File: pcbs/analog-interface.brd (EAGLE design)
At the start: 50 x 50 mm, 26 parts, among them U1 ISL3179EIBZ, U2 ATMEGA328P, U3 LM4120

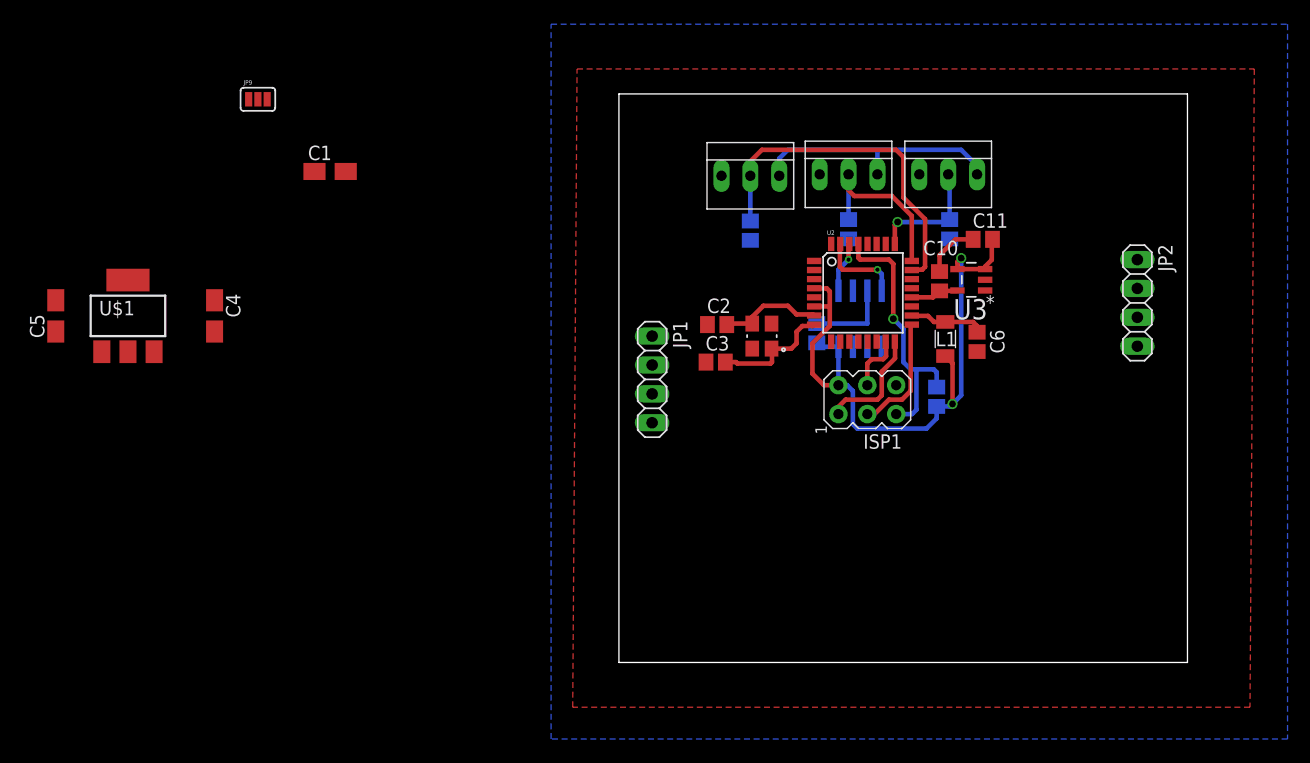
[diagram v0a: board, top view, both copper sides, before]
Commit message: Now uses external ADC and is long and thin.  Possibly too long...
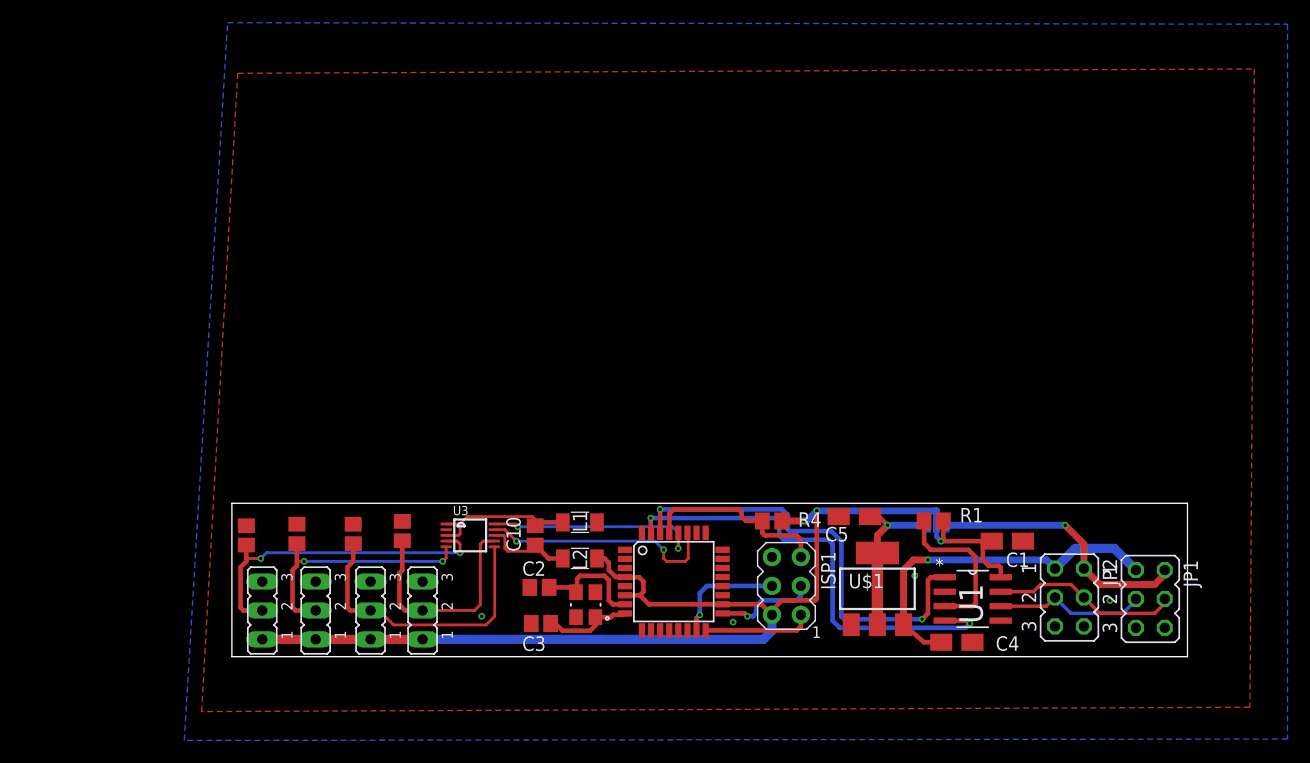
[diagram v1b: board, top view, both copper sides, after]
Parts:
- removed C11: 100nF, resistor:C0805
- added JP6: ADC3, jumper:JP2
- added L2: 10uH, resistor:L3216C
- C10: value 22nF -> 1uF
- C6, C7, C8, C9: value 100uF -> 1uF
- JP1, JP2: device pinhead:1X04 -> jumper:JP3Q
- JP3, JP4, JP5: device farnell-parts:3-MOLEX -> jumper:JP2
- U3: value LM4120 -> (none); device mountainsensing:SOT23-5 -> microbuilder:MSOP10
- moved C5 72.4 mm to (20.7, 12.8), turned to 0 degrees
- moved C4 71.3 mm to (29.7, 1.78), turned to 180 degrees
- moved JP9 70.5 mm to (27.9, 12.1), flipped to the bottom
- moved U$1 70.1 mm to (22.7, 6.48)
- moved C1 67.9 mm to (34.2, 10.7), turned to 180 degrees
- moved JP5 63.7 mm to (-21.8, 4.57), turned to 90 degrees
- moved JP4 60.6 mm to (-26.7, 4.57), turned to 90 degrees
- moved C9 58.9 mm to (-23.4, 11.3), flipped to the top, turned to 270 degrees
- moved JP3 57.5 mm to (-31.4, 4.57), turned to 90 degrees
- moved C8 55.4 mm to (-28.3, 11.3), flipped to the top, turned to 270 degrees
- moved C6 53.2 mm to (-19.1, 11.6), turned to 270 degrees
- moved C7 51.8 mm to (-32.8, 11.2), flipped to the top, turned to 270 degrees
- moved U3 49.5 mm to (-13.1, 11.2), turned to 270 degrees
- moved JP1 47.9 mm to (46.7, 5.59)
- moved C10 42.0 mm to (-7.37, 11.2)
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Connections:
- net 3V3 renamed 5V
- removed net AREF: C10.2, U2.20, U3.5
- removed net VIN: C1.+, C4.+, JP1.1, JP2.1, JP9.1, U$1.3
- new net 12V: C4.+, JP1.1, JP2.1, U$1.3
- new net 5V_IN: JP1.2, JP2.2, JP9.1
- new net ADC3: C6.2, JP6.2, U3.7
- new net SCL: U2.28, U3.10
- new net SDA: U2.27, U3.9
- net 485_N: now also JP1.4, JP2.4; no longer JP1.3, JP2.3
- net 485_P: now also JP1.3, JP2.3; no longer JP1.2, JP2.2
- net ADC0: now also U3.4; no longer U2.23
- net ADC1: now also U3.5; no longer U2.24
- net ADC2: now also U3.6; no longer U2.25
- net GND: now also JP1.5, JP1.6, JP2.5, JP2.6, JP6.3, L1.2; no longer JP1.4, JP2.4, U3.2
- net N$4: now also C10.1, U3.1, U3.3; no longer C6.2, U2.18
- net N$7: now also C10.2, L2.1, U3.8; no longer C10.1, C11.1
- net VCC: now also C1.+, JP6.1, L2.2, U2.18; no longer C11.2, L1.2, U3.3, U3.4
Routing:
- net RX: track 4.51 -> 38.9 mm, vias 1 -> 2
- net TX: track 7.44 -> 40.5 mm, vias 1 -> 2
- net 12V: track 0.00 -> 31.3 mm, vias 0 -> 1
- net VCC: track 81.5 -> 107.6 mm, vias 2 -> 3
- net 5V_IN: track 0.00 -> 23.4 mm, vias 0 -> 1
- net SDA: track 0.00 -> 21.1 mm, vias 0 -> 2
- net ADC3: track 0.00 -> 19.9 mm
- net SCL: track 0.00 -> 19.3 mm, vias 0 -> 2
- net 485_N: track 0.00 -> 16.5 mm
- net ADC2: track 10.7 -> 25.9 mm, vias 1 -> 0
- net 5V: track 0.00 -> 14.5 mm, vias 0 -> 1
- net 485_P: track 0.00 -> 13.4 mm
- net N$4: track 6.67 -> 13.5 mm
- net !RESET: track 23.6 -> 16.9 mm, vias 1 -> 0
- net N$1: track 7.33 -> 13.9 mm
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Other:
- board size 50 x 50 mm -> 84 x 13.5 mm

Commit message: Now has seperate AGND and AVCC 12V available on ADC headers lots of vias A bit shorter
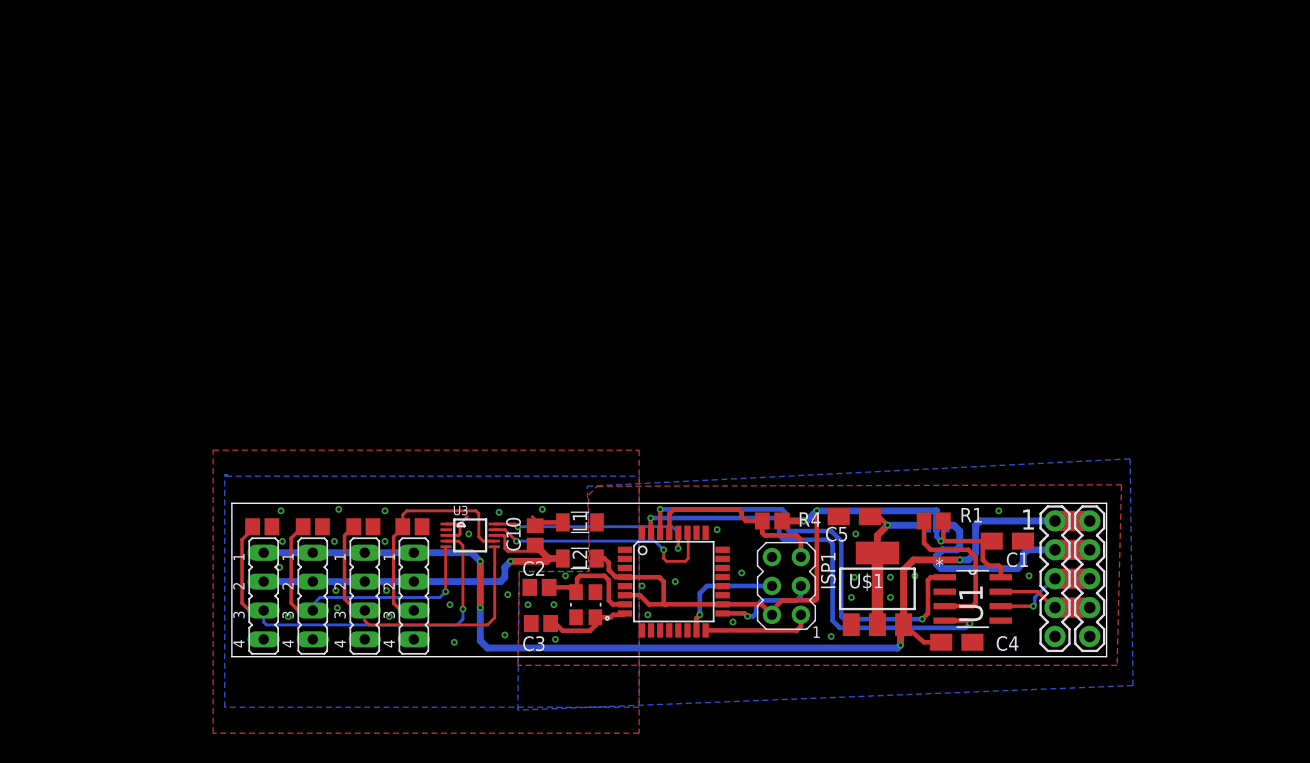
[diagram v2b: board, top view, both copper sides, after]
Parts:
- removed JP1, JP2: (no value), jumper:JP3Q
- added JP7, JP8: (no value), SparkFun-Connectors:1X05
- JP3: value ADC0 -> 0; device jumper:JP2 -> jumper:JP4
- JP4: value ADC1 -> 1; device jumper:JP2 -> jumper:JP4
- JP5: value ADC2 -> 2; device jumper:JP2 -> jumper:JP4
- JP6: value ADC3 -> 3; device jumper:JP2 -> jumper:JP4
- moved C7 1.59 mm to (-31.4, 11.9), turned to 180 degrees
- moved C8 1.53 mm to (-26.9, 11.9), turned to 180 degrees
- moved JP6 1.48 mm to (-18.0, 5.84), turned to 270 degrees
- moved JP5 1.37 mm to (-22.4, 5.84), turned to 270 degrees
- moved JP4 1.30 mm to (-26.9, 5.84), turned to 270 degrees
- moved JP3 1.28 mm to (-31.2, 5.84), turned to 270 degrees
- moved C9 1.09 mm to (-22.5, 11.9), turned to 180 degrees
- moved C6 0.97 mm to (-18.2, 11.9), turned to 180 degrees
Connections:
- removed net 12V: C4.+, JP1.1, JP2.1, U$1.3
- removed net N$4: C10.1, L1.1, U3.1, U3.3
- removed net N$7: C10.2, L2.1, U3.8
- new net 12V_IN: C4.+, JP3.1, JP4.1, JP5.1, JP6.1, JP7.1, JP8.1, U$1.3
- new net AGND: C10.1, C6.1, C7.1, C8.1, C9.1, JP3.4, JP4.4, JP5.4, JP6.4, L1.1, U3.1, U3.3
- new net AVCC: C10.2, JP3.2, JP4.2, JP5.2, JP6.2, L2.1, U3.8
- net 485_N: now also JP7.4, JP8.4; no longer JP1.4, JP2.4
- net 485_P: now also JP7.3, JP8.3; no longer JP1.3, JP2.3
- net 5V_IN: now also JP7.2, JP8.2; no longer JP1.2, JP2.2
- net ADC0: now also JP3.3; no longer JP3.2
- net ADC1: now also JP4.3; no longer JP4.2
- net ADC2: now also JP5.3; no longer JP5.2
- net ADC3: now also JP6.3; no longer JP6.2
- net GND: now also JP7.5, JP8.5; no longer C6.1, C7.1, C8.1, C9.1, JP1.5, JP1.6, JP2.5, JP2.6, JP3.3, JP4.3, JP5.3, JP6.3
- net VCC: no longer JP3.1, JP4.1, JP5.1, JP6.1
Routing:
- net 12V_IN: track 0.00 -> 93.9 mm, vias 0 -> 4
- net VCC: track 107.6 -> 63.5 mm
- net AVCC: track 0.00 -> 35.4 mm, vias 0 -> 1
- net 12V: track 31.3 -> 0.00 mm, vias 1 -> 0
- net N$4: track 13.5 -> 0.00 mm
- net N$7: track 8.22 -> 0.00 mm
- net 485_N: track 16.5 -> 8.40 mm
- net AGND: track 0.00 -> 7.80 mm, vias 0 -> 19
- net ADC0: track 28.8 -> 36.3 mm, vias 2 -> 1
- net 485_P: track 13.4 -> 9.19 mm, vias 0 -> 1
- net ADC1: track 22.2 -> 26.0 mm, vias 2 -> 1
- net 5V_IN: track 23.4 -> 20.7 mm, vias 1 -> 0
- net ADC2: track 25.9 -> 27.9 mm
- net ADC3: track 19.9 -> 20.7 mm
- added copper zone on layer 1, net AGND
- added copper zone on layer 16, net AGND
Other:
- board size 84 x 13.5 mm -> 76.9 x 13.5 mm
- board text added: "1"
